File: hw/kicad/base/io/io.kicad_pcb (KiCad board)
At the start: 2 copper layers, 45 x 45 mm, 10 parts, among them J1 SPI, J10 Conn_02x20_Odd_Even, J13 Conn_02x20_Odd_Even, J2 GPIO 1~4, J3 UART 2, J4 I2C, J5 GPIO 5~8, J6 CAN, J7 UART 1, J8 ADC 1~4

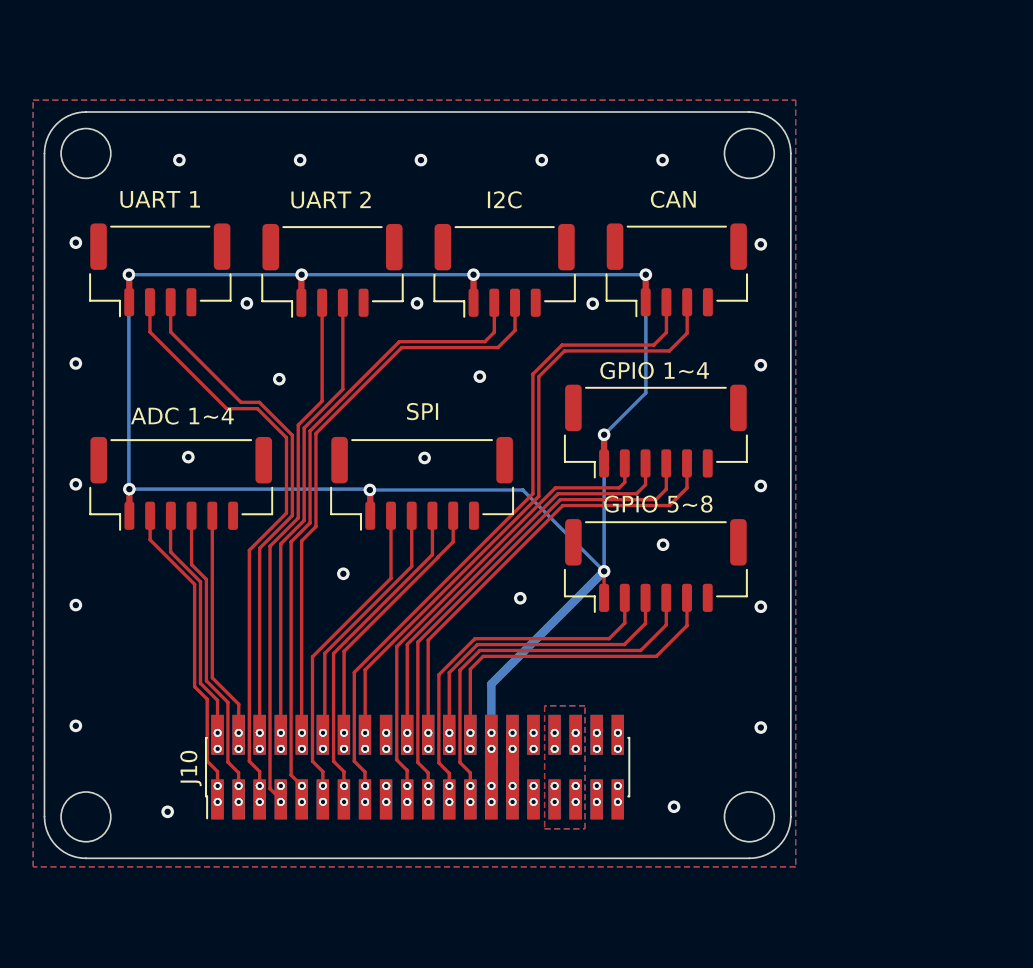
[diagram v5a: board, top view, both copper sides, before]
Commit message: 尽力改成40mmx40mm
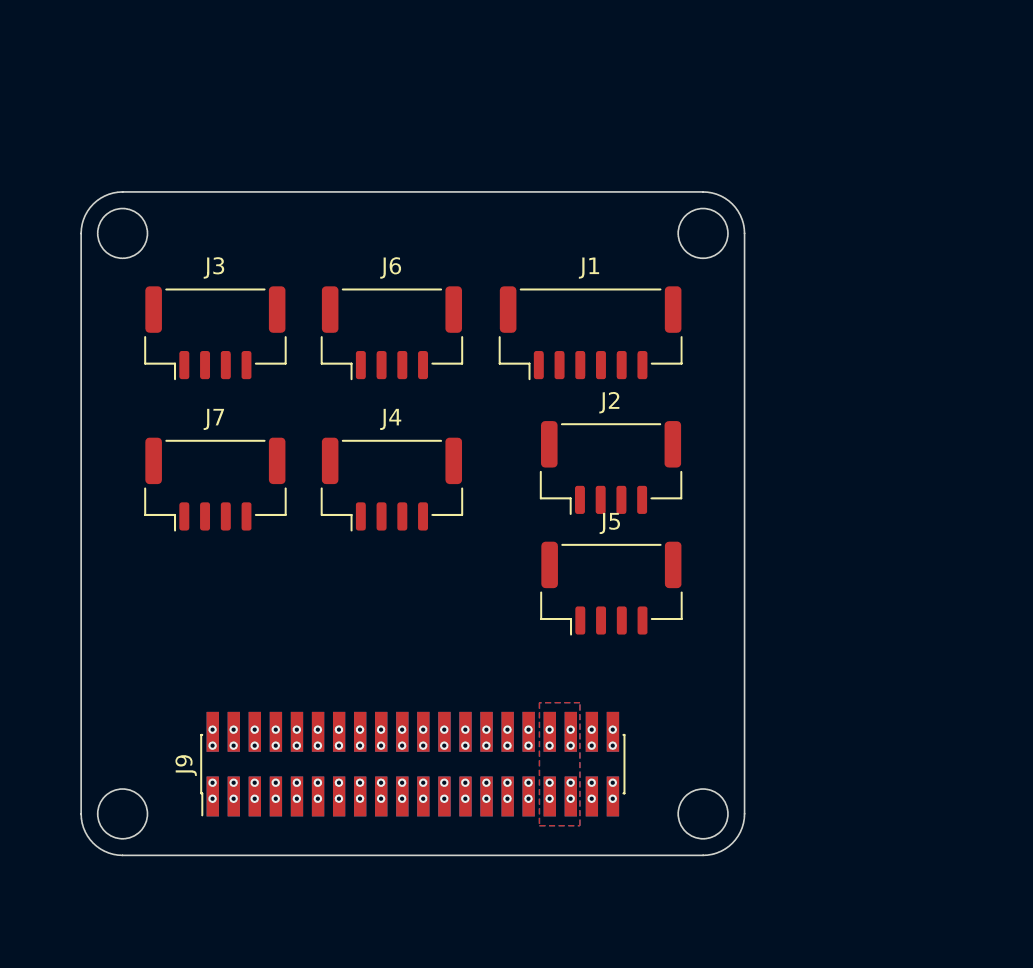
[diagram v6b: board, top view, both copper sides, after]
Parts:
- removed J13: Conn_02x20_Odd_Even, Connector_PinHeader_1.27mm:PinHeader_2x20_P1.27mm_Vertical_SMD
- removed J8: ADC 1~4, Connector_JST:JST_GH_BM06B-GHS-TBT_1x06-1MP_P1.25mm_Vertical
- added J9: TOP, Connector_PinHeader_1.27mm:PinHeader_2x20_P1.27mm_Vertical_SMD, F.Cu at (69.0, 73.1)
- J10: value Conn_02x20_Odd_Even -> BUTTOM; moved to B.Cu
- J2: value GPIO 1~4 -> PWM1; footprint Connector_JST:JST_GH_BM06B-GHS-TBT_1x06-1MP_P1.25mm_Vertical -> Connector_JST:JST_GH_BM04B-GHS-TBT_1x04-1MP_P1.25mm_Vertical
- J3: value UART 2 -> UART 1
- J5: value GPIO 5~8 -> PWM2; footprint Connector_JST:JST_GH_BM06B-GHS-TBT_1x06-1MP_P1.25mm_Vertical -> Connector_JST:JST_GH_BM04B-GHS-TBT_1x04-1MP_P1.25mm_Vertical
- J6: value CAN -> UART 2
- J7: value UART 1 -> ADC
- moved J6 17.6 mm to (67.8, 47.1)
- moved J4 14.6 mm to (67.8, 56.2)
- moved J1 13.6 mm to (79.7, 47.1)
- moved J7 13.3 mm to (57.1, 56.2)
- moved J3 8.00 mm to (57.1, 47.1)
- moved J2 3.48 mm to (81.0, 55.2)
- moved J5 3.01 mm to (81.0, 62.5)
- moved J10 0.34 mm to (69.0, 73.1), turned to -90 degrees
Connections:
- net /VBAT renamed /+BATT
- J10 pad 1: /ADC_1 -> /ADC_2
- J10 pad 10: /I2C_CLK -> /UART3_Rx
- J10 pad 11: /SPI_CS -> /I2C_CLK
- J10 pad 12: /SPI_CLK -> /I2C_SDA
- J10 pad 13: /SPI_MOSI -> /SPI_CLK
- J10 pad 14: /SPI_MISO -> /SPI_CS
- J10 pad 15: /CAN_H -> /SPI_MISO
- J10 pad 16: /CAN_L -> /SPI_MOSI
- J10 pad 17: /USB+ -> /GPIO_2
- J10 pad 18: /USB- -> /GPIO_1
- J10 pad 19: /GPIO_1 -> /GPIO_4
- J10 pad 2: /ADC_2 -> /ADC_1
- J10 pad 20: /GPIO_2 -> /GPIO_3
- J10 pad 21: /GPIO_3 -> /GPIO_6
- J10 pad 22: /GPIO_4 -> /GPIO_5
- J10 pad 23: /GPIO_5 -> /GPIO_8
- J10 pad 24: /GPIO_6 -> /GPIO_7
- J10 pad 25: /GPIO_7 -> /GPIO_10
- J10 pad 26: /GPIO_8 -> /GPIO_9
- J10 pad 29: /+5V -> +5V
- J10 pad 3: /ADC_3 -> /ADC_4
- J10 pad 30: /+5V -> +5V
- J10 pad 4: /ADC_4 -> /ADC_3
- J10 pad 5: /UART1_RX -> /UART1_Tx
- J10 pad 6: /UART1_TX -> /UART1_Rx
- J10 pad 7: /UART2_RX -> /UART2_Tx
- J10 pad 8: /UART2_TX -> /UART2_Rx
- J10 pad 9: /I2C_SDA -> /UART3_Tx
- J2 pad 2: /GPIO_1 -> +5V
- J2 pad 3: /GPIO_2 -> /GPIO_1
- J2 pad 4: /GPIO_3 -> GND
- J3 pad 2: /UART2_RX -> /UART1_RX
- J3 pad 3: /UART2_TX -> /UART1_TX
- J5 pad 2: /GPIO_5 -> +5V
- J5 pad 3: /GPIO_6 -> /GPIO_2
- J5 pad 4: /GPIO_7 -> GND
- J6 pad 2: /CAN_H -> /UART2_RX
- J6 pad 3: /CAN_L -> /UART2_TX
- J7 pad 2: /UART1_RX -> /ADC_3
- J7 pad 3: /UART1_TX -> /ADC_4
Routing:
- net +3.3V: track 127.4 -> 0.00 mm, vias 12 -> 4
- net /CAN_H: track 41.3 -> 0.00 mm, vias 2 -> 0
- net /CAN_L: track 37.7 -> 0.00 mm, vias 2 -> 0
- net /I2C_SDA: track 37.5 -> 0.00 mm
- net /UART1_RX: track 35.7 -> 0.00 mm, vias 2 -> 0
- net /I2C_CLK: track 34.7 -> 0.00 mm
- net /UART2_RX: track 31.5 -> 0.00 mm, vias 2 -> 0
- net /UART1_TX: track 30.6 -> 0.00 mm, vias 2 -> 0
- net /GPIO_3: track 30.1 -> 0.00 mm
- net /GPIO_1: track 28.5 -> 0.00 mm
- net /UART2_TX: track 27.6 -> 0.00 mm, vias 2 -> 0
- net /GPIO_4: track 26.6 -> 0.00 mm
- net /GPIO_2: track 25.0 -> 0.00 mm
- net /GPIO_7: track 23.2 -> 0.00 mm
- net /GPIO_5: track 21.8 -> 0.00 mm
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- added copper zone on B.Cu, net (none)
- added copper zone on F.Cu, net (none)
- removed copper zone on B.Cu, net /+BATT
- removed copper zone on F.Cu, net /+BATT
- removed copper zone on B.Cu, net GND
- removed copper zone on F.Cu, net GND
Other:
- board size 45 x 45 mm -> 40 x 40 mm

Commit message: Merge from normal
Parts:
- removed J9: TOP, Connector_PinHeader_1.27mm:PinHeader_2x20_P1.27mm_Vertical_SMD
- added J13: Conn_02x20_Odd_Even, Connector_PinHeader_1.27mm:PinHeader_2x20_P1.27mm_Vertical_SMD, B.Cu at (69.3, 73.3)
- added J8: ADC 1~4, Connector_JST:JST_GH_BM06B-GHS-TBT_1x06-1MP_P1.25mm_Vertical, F.Cu at (55.1, 56.2)
- J10: value BUTTOM -> Conn_02x20_Odd_Even; moved to F.Cu
- J2: value PWM1 -> GPIO 1~4; footprint Connector_JST:JST_GH_BM04B-GHS-TBT_1x04-1MP_P1.25mm_Vertical -> Connector_JST:JST_GH_BM06B-GHS-TBT_1x06-1MP_P1.25mm_Vertical
- J3: value UART 1 -> UART 2
- J5: value PWM2 -> GPIO 5~8; footprint Connector_JST:JST_GH_BM04B-GHS-TBT_1x04-1MP_P1.25mm_Vertical -> Connector_JST:JST_GH_BM06B-GHS-TBT_1x06-1MP_P1.25mm_Vertical
- J6: value UART 2 -> CAN
- J7: value ADC -> UART 1
- moved J6 17.6 mm to (84.9, 43.3)
- moved J4 14.6 mm to (74.6, 43.3)
- moved J1 13.6 mm to (69.6, 56.2)
- moved J7 13.3 mm to (53.8, 43.3)
- moved J3 8.00 mm to (64.2, 43.3)
- moved J2 3.48 mm to (83.7, 53.0)
- moved J5 3.01 mm to (83.7, 61.1)
- moved J10 0.34 mm to (69.3, 73.3), turned to 90 degrees
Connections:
- net /+BATT renamed /VBAT
- J10 pad 1: /ADC_2 -> /ADC_1
- J10 pad 10: /UART3_Rx -> /I2C_CLK
- J10 pad 11: /I2C_CLK -> /SPI_CS
- J10 pad 12: /I2C_SDA -> /SPI_CLK
- J10 pad 13: /SPI_CLK -> /SPI_MOSI
- J10 pad 14: /SPI_CS -> /SPI_MISO
- J10 pad 15: /SPI_MISO -> /CAN_H
- J10 pad 16: /SPI_MOSI -> /CAN_L
- J10 pad 17: /GPIO_2 -> /USB+
- J10 pad 18: /GPIO_1 -> /USB-
- J10 pad 19: /GPIO_4 -> /GPIO_1
- J10 pad 2: /ADC_1 -> /ADC_2
- J10 pad 20: /GPIO_3 -> /GPIO_2
- J10 pad 21: /GPIO_6 -> /GPIO_3
- J10 pad 22: /GPIO_5 -> /GPIO_4
- J10 pad 23: /GPIO_8 -> /GPIO_5
- J10 pad 24: /GPIO_7 -> /GPIO_6
- J10 pad 25: /GPIO_10 -> /GPIO_7
- J10 pad 26: /GPIO_9 -> /GPIO_8
- J10 pad 29: +5V -> /+5V
- J10 pad 3: /ADC_4 -> /ADC_3
- J10 pad 30: +5V -> /+5V
- J10 pad 4: /ADC_3 -> /ADC_4
- J10 pad 5: /UART1_Tx -> /UART1_RX
- J10 pad 6: /UART1_Rx -> /UART1_TX
- J10 pad 7: /UART2_Tx -> /UART2_RX
- J10 pad 8: /UART2_Rx -> /UART2_TX
- J10 pad 9: /UART3_Tx -> /I2C_SDA
- J2 pad 2: +5V -> /GPIO_1
- J2 pad 3: /GPIO_1 -> /GPIO_2
- J2 pad 4: GND -> /GPIO_3
- J3 pad 2: /UART1_RX -> /UART2_RX
- J3 pad 3: /UART1_TX -> /UART2_TX
- J5 pad 2: +5V -> /GPIO_5
- J5 pad 3: /GPIO_2 -> /GPIO_6
- J5 pad 4: GND -> /GPIO_7
- J6 pad 2: /UART2_RX -> /CAN_H
- J6 pad 3: /UART2_TX -> /CAN_L
- J7 pad 2: /ADC_3 -> /UART1_RX
- J7 pad 3: /ADC_4 -> /UART1_TX
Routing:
- net +3.3V: track 0.00 -> 128.7 mm, vias 4 -> 12
- net /CAN_H: track 0.00 -> 41.3 mm, vias 0 -> 2
- net /CAN_L: track 0.00 -> 37.7 mm, vias 0 -> 2
- net /I2C_SDA: track 0.00 -> 37.5 mm
- net /UART1_RX: track 0.00 -> 35.7 mm, vias 0 -> 2
- net /I2C_CLK: track 0.00 -> 34.7 mm
- net /UART2_RX: track 0.00 -> 31.5 mm, vias 0 -> 2
- net /UART1_TX: track 0.00 -> 30.6 mm, vias 0 -> 2
- net /GPIO_3: track 0.00 -> 30.1 mm
- net /GPIO_1: track 0.00 -> 28.5 mm
- net /UART2_TX: track 0.00 -> 27.6 mm, vias 0 -> 2
- net /GPIO_4: track 0.00 -> 26.6 mm
- net /GPIO_2: track 0.00 -> 25.0 mm
- net /GPIO_7: track 0.00 -> 23.2 mm
- net /GPIO_5: track 0.00 -> 21.8 mm
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- added copper zone on B.Cu, net /VBAT
- added copper zone on F.Cu, net /VBAT
- added copper zone on B.Cu, net GND
- added copper zone on F.Cu, net GND
- removed copper zone on B.Cu, net (none)
- removed copper zone on F.Cu, net (none)
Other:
- board size 40 x 40 mm -> 45 x 45 mm

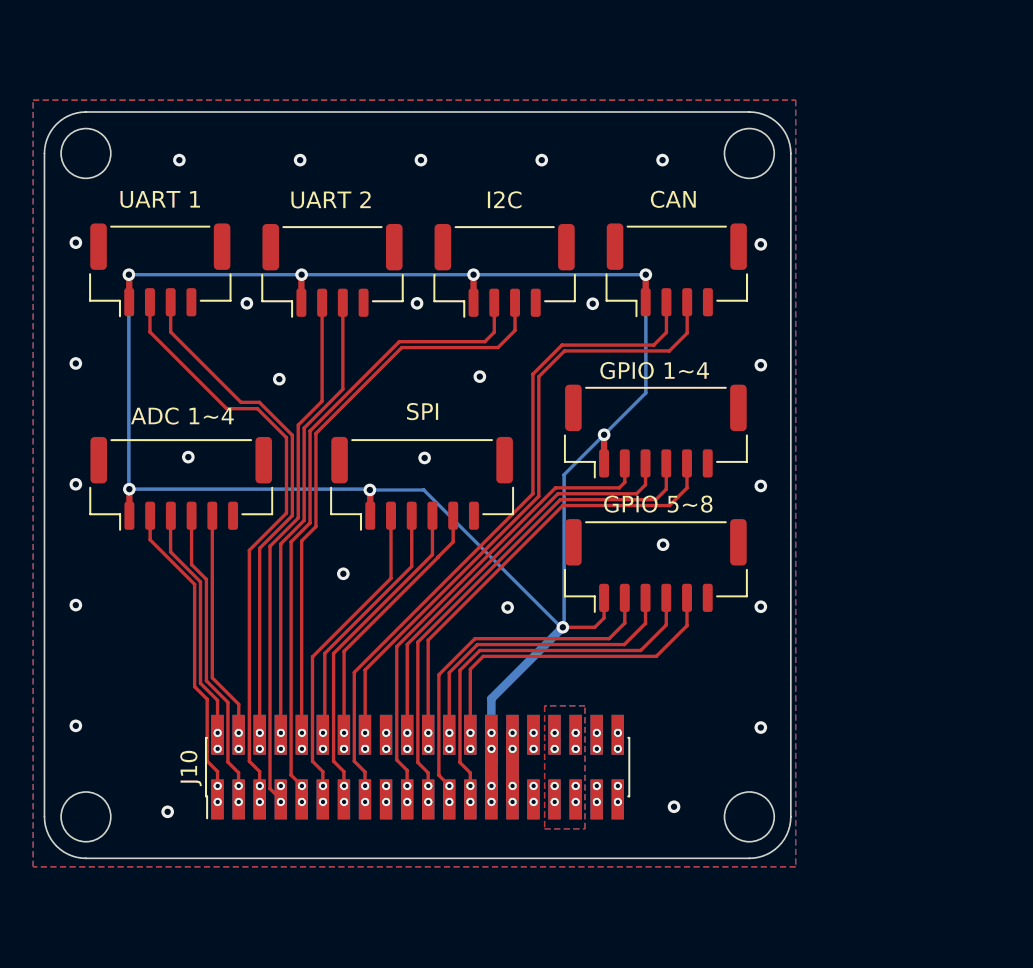
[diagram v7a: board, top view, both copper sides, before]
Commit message: 更新power16v一些错误
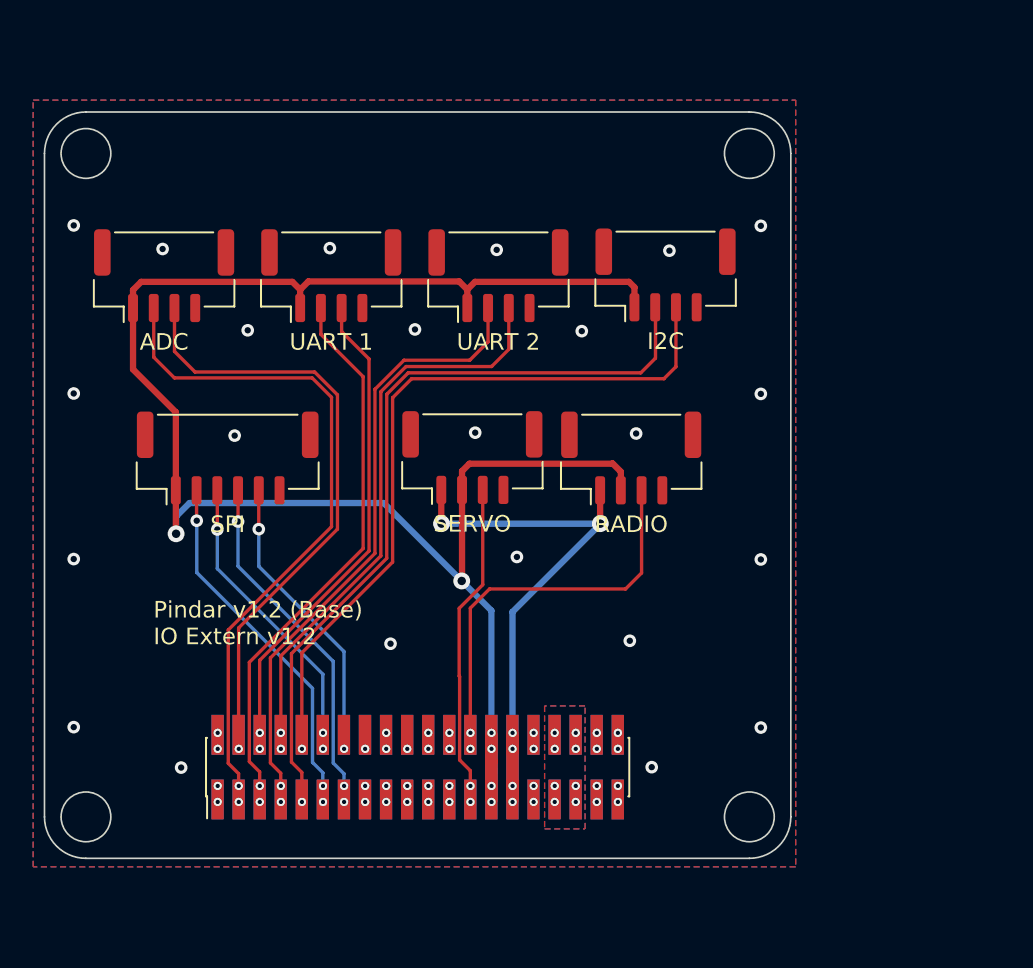
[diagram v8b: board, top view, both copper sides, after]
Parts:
- removed J10, J13: Conn_02x20_Odd_Even, Connector_PinHeader_1.27mm:PinHeader_2x20_P1.27mm_Vertical_SMD
- added J9: BUTTOM, Connector_PinHeader_1.27mm:PinHeader_2x20_P1.27mm_Vertical_SMD, B.Cu at (69.3, 73.3)
- J2: value GPIO 1~4 -> SERVO; footprint Connector_JST:JST_GH_BM06B-GHS-TBT_1x06-1MP_P1.25mm_Vertical -> Connector_JST:JST_GH_BM04B-GHS-TBT_1x04-1MP_P1.25mm_Vertical
- J3: value UART 2 -> UART 1
- J5: value GPIO 5~8 -> RADIO; footprint Connector_JST:JST_GH_BM06B-GHS-TBT_1x06-1MP_P1.25mm_Vertical -> Connector_JST:JST_GH_BM04B-GHS-TBT_1x04-1MP_P1.25mm_Vertical
- J6: value CAN -> UART 2
- J7: value UART 1 -> ADC
- J8: value ADC 1~4 -> TOP; footprint Connector_JST:JST_GH_BM06B-GHS-TBT_1x06-1MP_P1.25mm_Vertical -> Connector_PinHeader_1.27mm:PinHeader_2x20_P1.27mm_Vertical_SMD
- moved J8 22.3 mm to (69.3, 73.3), turned to 90 degrees
- moved J1 11.8 mm to (57.9, 54.6)
- moved J2 11.2 mm to (72.6, 54.6)
- moved J6 10.8 mm to (74.2, 43.6)
- moved J4 9.71 mm to (84.3, 43.6)
- moved J5 6.65 mm to (82.2, 54.6)
- moved J7 0.42 mm to (54.0, 43.6)
- moved J3 0.33 mm to (64.1, 43.6)
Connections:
- J2 pad 1: +3.3V -> +5V
- J2 pad 2: /GPIO_1 -> +3.3V
- J2 pad 3: /GPIO_2 -> /GPIO_11
- J2 pad 4: /GPIO_3 -> GND
- J3 pad 2: /UART2_RX -> /UART1_Rx
- J3 pad 3: /UART2_TX -> /UART1_Tx
- J5 pad 1: +3.3V -> +5V
- J5 pad 2: /GPIO_5 -> +3.3V
- J5 pad 3: /GPIO_6 -> /GPIO_12
- J5 pad 4: /GPIO_7 -> GND
- J6 pad 2: /CAN_H -> /UART2_Rx
- J6 pad 3: /CAN_L -> /UART2_Tx
- J7 pad 2: /UART1_RX -> /ADC_3
- J7 pad 3: /UART1_TX -> /ADC_4
- J8 pad 1: +3.3V -> /ADC_1
- J8 pad 2: /ADC_1 -> /ADC_2
- J8 pad 3: /ADC_2 -> /ADC_3
- J8 pad 4: /ADC_3 -> /ADC_4
- J8 pad 5: /ADC_4 -> /UART1_Rx
- J8 pad 6: GND -> /UART1_Tx
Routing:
- net /CAN_H: track 41.3 -> 0.00 mm, vias 2 -> 0
- net /CAN_L: track 37.7 -> 0.00 mm, vias 2 -> 0
- net /UART2_Rx: track 0.00 -> 37.6 mm, vias 0 -> 2
- net +5V: track 0.00 -> 36.4 mm, vias 0 -> 6
- net /UART1_RX: track 35.7 -> 0.00 mm, vias 2 -> 0
- net /UART2_Tx: track 0.00 -> 34.3 mm, vias 0 -> 2
- net /UART1_Rx: track 0.00 -> 33.8 mm, vias 0 -> 2
- net /UART2_RX: track 31.5 -> 0.00 mm, vias 2 -> 0
- net /UART1_TX: track 30.6 -> 0.00 mm, vias 2 -> 0
- net /GPIO_3: track 30.1 -> 0.00 mm
- net /UART1_Tx: track 0.00 -> 29.1 mm, vias 0 -> 2
- net /GPIO_1: track 28.5 -> 0.00 mm
- net /UART2_TX: track 27.6 -> 0.00 mm, vias 2 -> 0
- net /GPIO_4: track 26.6 -> 0.00 mm
- net /GPIO_2: track 25.0 -> 0.00 mm, vias 2 -> 1
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- added copper zone on B.Cu, net /+BATT
- added copper zone on F.Cu, net /+BATT
- removed copper zone on B.Cu, net /VBAT
- removed copper zone on F.Cu, net /VBAT
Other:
- board text added: "Pindar v1.2 (Base) IO Extern v1.2"
